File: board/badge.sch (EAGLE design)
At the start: 46 parts, among them IC1 STM32F030F4, IC2 UBLOX_MAX, IC3 RFM69HW, IC4 MCP1640, J2 20-0096, J3 SWD_PTH_SHROUD, X1 RADIOMETRIX-MTX2, X2 SMA-142-0701-851/861, X3 091OLED

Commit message: Tied Reset pin on GPS to VCC
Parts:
- removed JP2: (no value), SparkFun-Connectors:M06SMD
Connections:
- net +3V3: now also IC2.9_V_RESET
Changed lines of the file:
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@@
 <?xml version="1.0" encoding="utf-8"?>
 <!DOCTYPE eagle SYSTEM "eagle.dtd">
-<eagle version="6.5.0">
+<eagle version="6.4">
 <drawing>
 <settings>
@@
 <part name="TP3" library="testpad" deviceset="PTR1" device="B2,54"/>
 <part name="J2" library="ukhas" deviceset="3.5MMJACKSMD" device="" value="20-0096"/>
-<part name="JP2" library="SparkFun-Connectors" deviceset="M06" device="SMD"/>
 <part name="R8" library="rcl" deviceset="R-EU_" device="R0603" value="10k"/>
 <part name="R9" library="rcl" deviceset="R-EU_" device="R0603" value="10k"/>
@@
 <instance part="TP3" gate="G$1" x="27.94" y="119.38" rot="R180"/>
 <instance part="J2" gate="G$1" x="22.86" y="53.34" rot="R180"/>
-<instance part="JP2" gate="G$1" x="73.66" y="66.04" rot="R180"/>
 <instance part="R8" gate="G$1" x="-7.62" y="114.3" rot="R180"/>
 <instance part="R9" gate="G$1" x="2.54" y="114.3" rot="R180"/>
@@
 <wire x1="43.18" y1="96.52" x2="43.18" y2="91.44" width="0.1524" layer="91"/>
 <junction x="43.18" y="91.44"/>
-</segment>
-<segment>
+<wire x1="43.18" y1="86.36" x2="43.18" y2="81.28" width="0.1524" layer="91"/>
+<pinref part="IC2" gate="G$1" pin="9_V_RESET"/>
+<wire x1="43.18" y1="81.28" x2="48.26" y2="81.28" width="0.1524" layer="91"/>
+</segment>
+<segment>

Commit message: started rev2
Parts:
- added C13, C14: 1u, rcl:C-EUC0603
- added R10: 220k, rcl:R-EU_R0603
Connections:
- removed net O_RES: IC1.PA1, X3.RES
- new net N$22: C13.2, R10.1, X3.RES
- new net N$23: C14.2, J2.4
- new net O_DC: IC1.PA1, X3.D/C
- net +3V3: now also R10.2
- net 0V: now also C13.1; no longer X3.D/C
- net ADC1: now also C14.1; no longer J2.4
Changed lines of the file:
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@@
 <?xml version="1.0" encoding="utf-8"?>
 <!DOCTYPE eagle SYSTEM "eagle.dtd">
-<eagle version="6.4">
+<eagle version="6.5.0">
 <drawing>
 <settings>
@@
 <part name="+3V13" library="supply1" deviceset="+3V3" device=""/>
 <part name="GND29" library="supply1" deviceset="0V" device=""/>
-<part name="GND30" library="supply1" deviceset="0V" device=""/>
 <part name="GND31" library="supply1" deviceset="0V" device=""/>
 <part name="R3" library="rcl" deviceset="R-EU_" device="R0603" value="1k"/>
@@
 <part name="+3V17" library="supply1" deviceset="+3V3" device=""/>
 <part name="GND21" library="supply1" deviceset="0V" device=""/>
+<part name="C13" library="rcl" deviceset="C-EU" device="C0603" value="1u"/>
+<part name="R10" library="rcl" deviceset="R-EU_" device="R0603" value="220k"/>
+<part name="GND30" library="supply1" deviceset="0V" device=""/>
+<part name="+3V18" library="supply1" deviceset="+3V3" device=""/>
+<part name="C14" library="rcl" deviceset="C-EU" device="C0603" value="1u"/>
 </parts>
 <sheets>
@@
 <instance part="+3V13" gate="G$1" x="-71.12" y="33.02"/>
 <instance part="GND29" gate="1" x="-50.8" y="5.08"/>
-<instance part="GND30" gate="1" x="5.08" y="10.16" rot="R270"/>
 <instance part="GND31" gate="1" x="-30.48" y="43.18" rot="R270"/>
 <instance part="R3" gate="G$1" x="-22.86" y="43.18" rot="R180"/>
@@
 <instance part="+3V17" gate="G$1" x="-15.24" y="114.3" rot="R90"/>
 <instance part="GND21" gate="1" x="10.16" y="114.3" rot="R90"/>
+<instance part="C13" gate="G$1" x="-7.62" y="15.24" rot="R90"/>
+<instance part="R10" gate="G$1" x="-7.62" y="20.32" rot="R180"/>
+<instance part="GND30" gate="1" x="-12.7" y="15.24" rot="R270"/>
+<instance part="+3V18" gate="G$1" x="-15.24" y="20.32" rot="R90"/>
+<instance part="C14" gate="G$1" x="7.62" y="58.42" rot="R90"/>
 </instances>
 <busses>
@@
 <pinref part="+3V17" gate="G$1" pin="+3V3"/>
 </segment>
+<segment>
+<pinref part="R10" gate="G$1" pin="2"/>
+<pinref part="+3V18" gate="G$1" pin="+3V3"/>
+</segment>
 </net>
 <net name="0V" class="0">
@@
 </segment>
 <segment>
-<pinref part="X3" gate="G$1" pin="D/C"/>
-<pinref part="GND30" gate="1" pin="0V"/>
-</segment>
-<segment>
 <pinref part="R3" gate="G$1" pin="2"/>
 <pinref part="GND31" gate="1" pin="0V"/>
@@
 <pinref part="R9" gate="G$1" pin="1"/>
 <pinref part="GND21" gate="1" pin="0V"/>
+</segment>
+<segment>
+<pinref part="C13" gate="G$1" pin="1"/>
+<pinref part="GND30" gate="1" pin="0V"/>
 </segment>
 </net>
@@
 </segment>
 <segment>
-<wire x1="12.7" y1="58.42" x2="2.54" y2="58.42" width="0.1524" layer="91"/>
-<label x="2.54" y="58.42" size="1.778" layer="95"/>
-<pinref part="J2" gate="G$1" pin="4"/>
+<pinref part="C14" gate="G$1" pin="1"/>
+<wire x1="5.08" y1="58.42" x2="0" y2="58.42" width="0.1524" layer="91"/>
+<label x="0" y="58.42" size="1.778" layer="95"/>
 </segment>
 </net>
@@
 </segment>
 </net>
-<net name="O_RES" class="0">
-<segment>
-<pinref part="X3" gate="G$1" pin="RES"/>
-<wire x1="7.62" y1="15.24" x2="-5.08" y2="15.24" width="0.1524" layer="91"/>
-<label x="-2.54" y="15.24" size="1.778" layer="95"/>
-</segment>
+<net name="O_DC" class="0">
 <segment>
 <pinref part="IC1" gate="G$1" pin="PA1"/>
 <wire x1="-10.16" y1="104.14" x2="0" y2="104.14" width="0.1524" layer="91"/>
 <label x="-5.08" y="104.14" size="1.778" layer="95"/>
+</segment>
+<segment>
+<pinref part="X3" gate="G$1" pin="D/C"/>
+<wire x1="7.62" y1="10.16" x2="-5.08" y2="10.16" width="0.1524" layer="91"/>
+<label x="-2.54" y="10.16" size="1.778" layer="95"/>
 </segment>
 </net>
@@
 </segment>
 </net>
+<net name="N$22" class="0">
+<segment>
+<pinref part="X3" gate="G$1" pin="RES"/>
+<pinref part="C13" gate="G$1" pin="2"/>
+<wire x1="7.62" y1="15.24" x2="0" y2="15.24" width="0.1524" layer="91"/>
+<pinref part="R10" gate="G$1" pin="1"/>
+<wire x1="0" y1="15.24" x2="-2.54" y2="15.24" width="0.1524" layer="91"/>
+<wire x1="-2.54" y1="20.32" x2="0" y2="20.32" width="0.1524" layer="91"/>
+<wire x1="0" y1="20.32" x2="0" y2="15.24" width="0.1524" layer="91"/>
+<junction x="0" y="15.24"/>
+</segment>
+</net>
+<net name="N$23" class="0">
+<segment>
+<pinref part="J2" gate="G$1" pin="4"/>
+<pinref part="C14" gate="G$1" pin="2"/>
+</segment>
+</net>

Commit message: rev2 almost done
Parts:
- added R11: 10k, rcl:R-EU_R0603
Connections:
- new net N$24: C14.1, R11.2
- net ADC1: now also R11.1; no longer C14.1
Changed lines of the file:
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@@
 <part name="+3V18" library="supply1" deviceset="+3V3" device=""/>
 <part name="C14" library="rcl" deviceset="C-EU" device="C0603" value="1u"/>
+<part name="R11" library="rcl" deviceset="R-EU_" device="R0603" value="10k"/>
 </parts>
 <sheets>
@@
 <instance part="+3V18" gate="G$1" x="-15.24" y="20.32" rot="R90"/>
 <instance part="C14" gate="G$1" x="7.62" y="58.42" rot="R90"/>
+<instance part="R11" gate="G$1" x="7.62" y="63.5" rot="R180"/>
 </instances>
 <busses>
@@
 </segment>
 <segment>
-<pinref part="C14" gate="G$1" pin="1"/>
-<wire x1="5.08" y1="58.42" x2="0" y2="58.42" width="0.1524" layer="91"/>
-<label x="0" y="58.42" size="1.778" layer="95"/>
+<pinref part="R11" gate="G$1" pin="1"/>
+<wire x1="12.7" y1="63.5" x2="20.32" y2="63.5" width="0.1524" layer="91"/>
+<label x="12.7" y="63.5" size="1.778" layer="95"/>
 </segment>
 </net>
@@
 </segment>
 </net>
+<net name="N$24" class="0">
+<segment>
+<pinref part="C14" gate="G$1" pin="1"/>
+<pinref part="R11" gate="G$1" pin="2"/>
+<wire x1="5.08" y1="58.42" x2="2.54" y2="58.42" width="0.1524" layer="91"/>
+<wire x1="2.54" y1="58.42" x2="2.54" y2="63.5" width="0.1524" layer="91"/>
+</segment>
+</net>

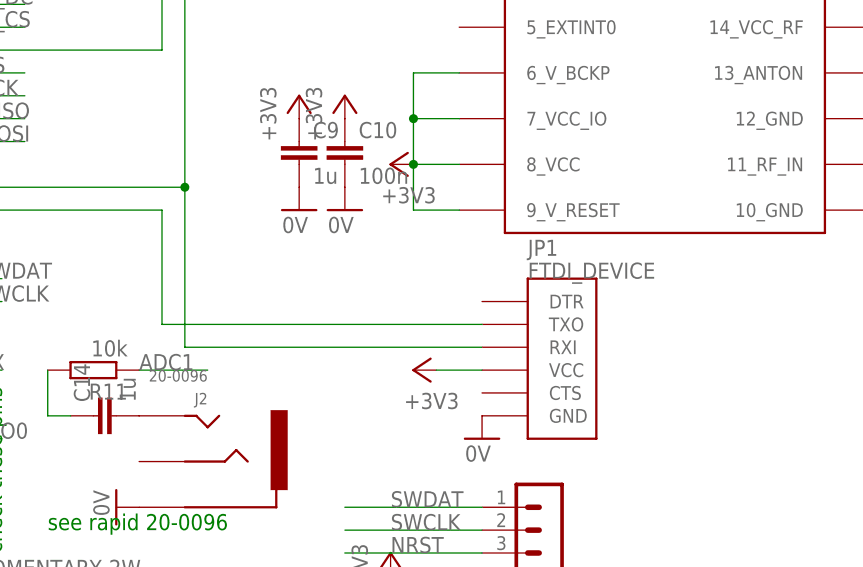
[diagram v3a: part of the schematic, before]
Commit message: switching tx/rx on ftdi
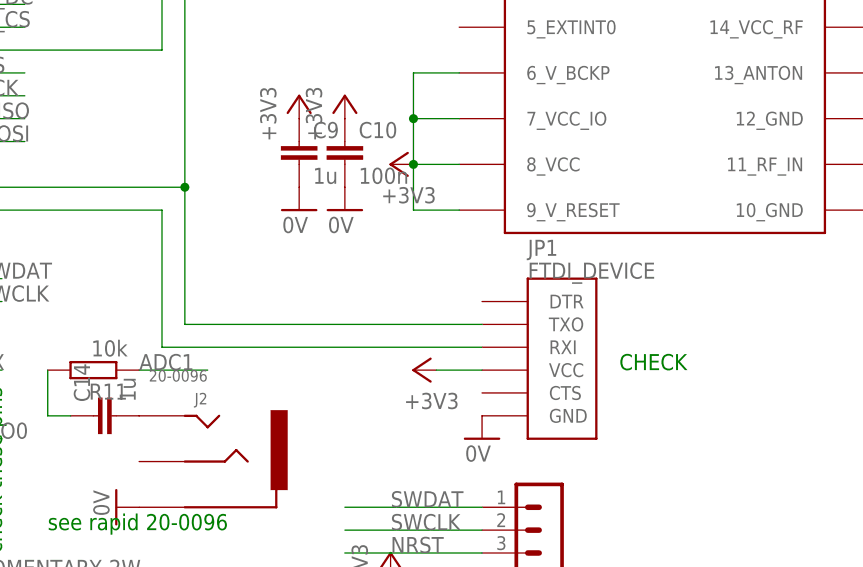
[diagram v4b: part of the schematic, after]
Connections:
- net N$8: now also JP1.TXO; no longer JP1.RXI
- net N$9: now also JP1.RXI; no longer JP1.TXO
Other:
- note added: "CHECK"
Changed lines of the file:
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@@
 <text x="-78.74" y="106.68" size="1.778" layer="91" rot="R180">3801305</text>
 <text x="-7.62" y="40.64" size="1.778" layer="91" rot="R180">3801305</text>
+<text x="66.04" y="63.5" size="1.778" layer="91">CHECK</text>
 </plain>
 <instances>
@@
 <net name="N$8" class="0">
 <segment>
-<pinref part="JP1" gate="G$1" pin="RXI"/>
-<wire x1="50.8" y1="66.04" x2="17.78" y2="66.04" width="0.1524" layer="91"/>
-<wire x1="17.78" y1="66.04" x2="17.78" y2="83.82" width="0.1524" layer="91"/>
 <pinref part="IC1" gate="G$1" pin="PA9"/>
 <pinref part="IC2" gate="G$1" pin="3_RXD1"/>
+<wire x1="17.78" y1="68.58" x2="17.78" y2="83.82" width="0.1524" layer="91"/>
 <wire x1="17.78" y1="83.82" x2="-10.16" y2="83.82" width="0.1524" layer="91"/>
 <wire x1="48.26" y1="111.76" x2="17.78" y2="111.76" width="0.1524" layer="91"/>
 <wire x1="17.78" y1="111.76" x2="17.78" y2="83.82" width="0.1524" layer="91"/>
 <junction x="17.78" y="83.82"/>
+<pinref part="JP1" gate="G$1" pin="TXO"/>
+<wire x1="50.8" y1="68.58" x2="17.78" y2="68.58" width="0.1524" layer="91"/>
 </segment>
 </net>
 <net name="N$9" class="0">
 <segment>
-<pinref part="JP1" gate="G$1" pin="TXO"/>
-<wire x1="50.8" y1="68.58" x2="15.24" y2="68.58" width="0.1524" layer="91"/>
-<wire x1="15.24" y1="68.58" x2="15.24" y2="81.28" width="0.1524" layer="91"/>
+<wire x1="15.24" y1="66.04" x2="15.24" y2="81.28" width="0.1524" layer="91"/>
 <pinref part="IC1" gate="G$1" pin="PA10"/>
 <wire x1="15.24" y1="81.28" x2="-10.16" y2="81.28" width="0.1524" layer="91"/>
-</segment>
-</net>
+<pinref part="JP1" gate="G$1" pin="RXI"/>
+<wire x1="50.8" y1="66.04" x2="15.24" y2="66.04" width="0.1524" layer="91"/>
+</segment>
+</net>
